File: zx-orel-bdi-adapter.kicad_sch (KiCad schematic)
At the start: 32 parts, among them J1 Barrel_Jack_Switch, J2 DB9_Male, SW1 SW_Push_Dual, SW2 SW_DPDT_x2, U1 74LS30, U2 74LS27, U3 74LS04, U4 74LS640, U5 28C256

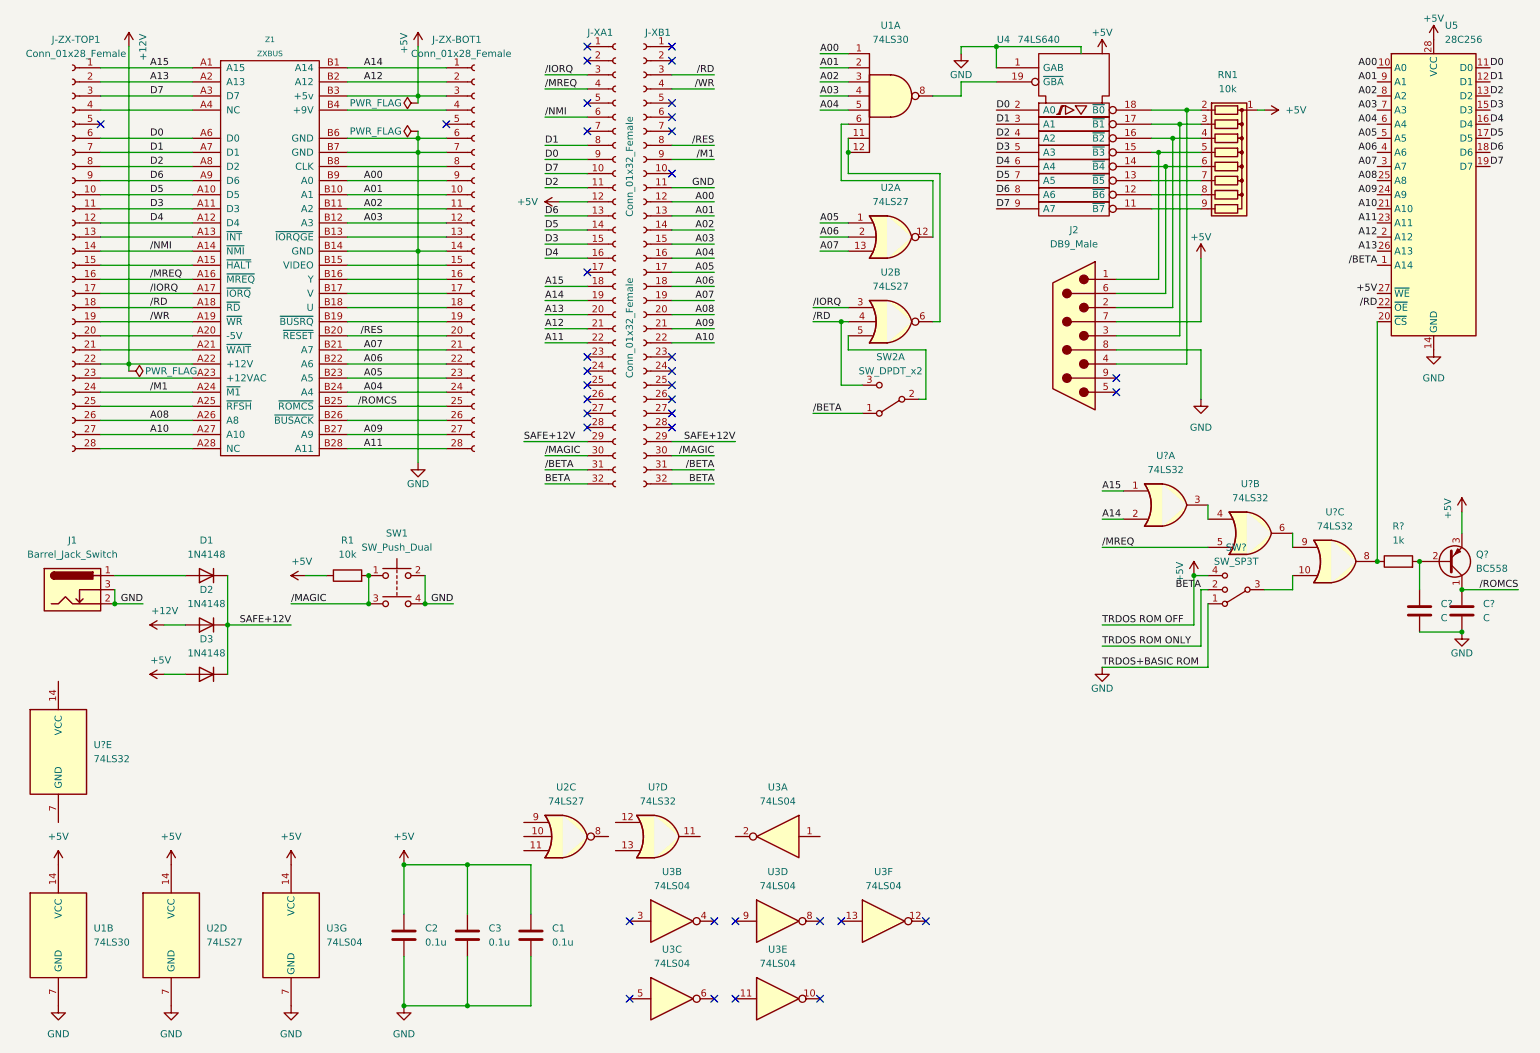
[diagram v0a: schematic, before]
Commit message: fixed romcs part
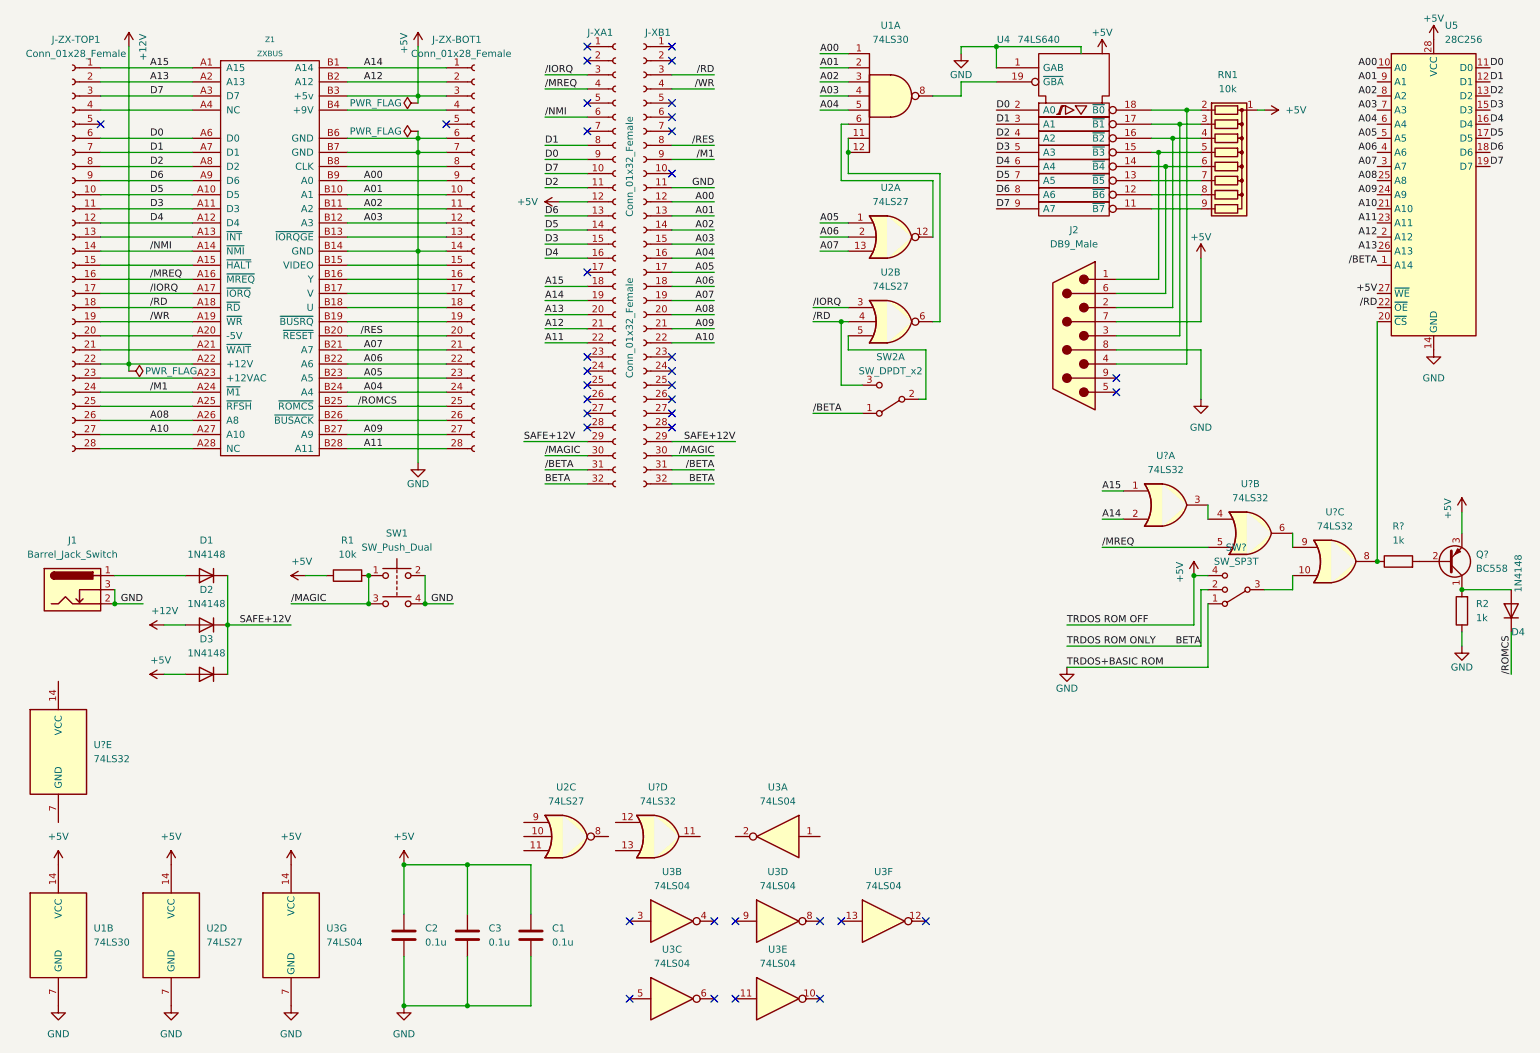
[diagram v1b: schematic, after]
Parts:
- removed C? (x2): C, symbol Device:C
- added D4: 1N4148, Diode_THT:D_DO-35_SOD27_P7.62mm_Horizontal, symbol Diode:1N4148
- added R2: 1k, symbol Device:R
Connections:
- net GND: now also R2.1
- net /ROMCS: now also D4.1 (K); no longer Q?.1 (C)
- new net: D4.2 (A), Q?.1 (C), R2.2

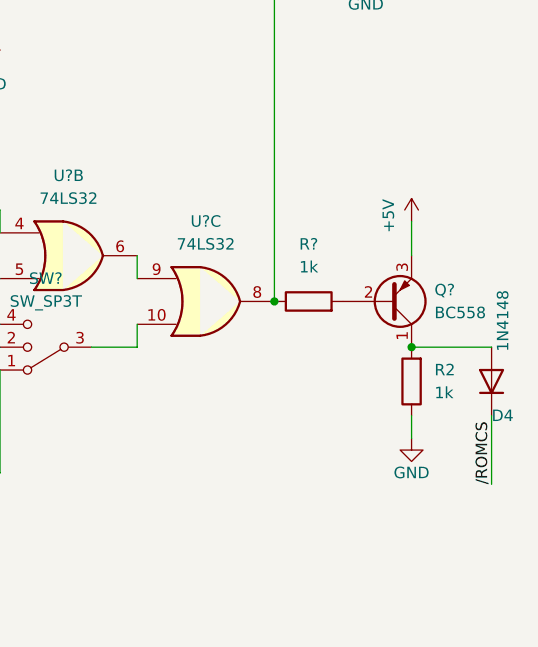
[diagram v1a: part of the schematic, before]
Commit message: changed bc558 schematic
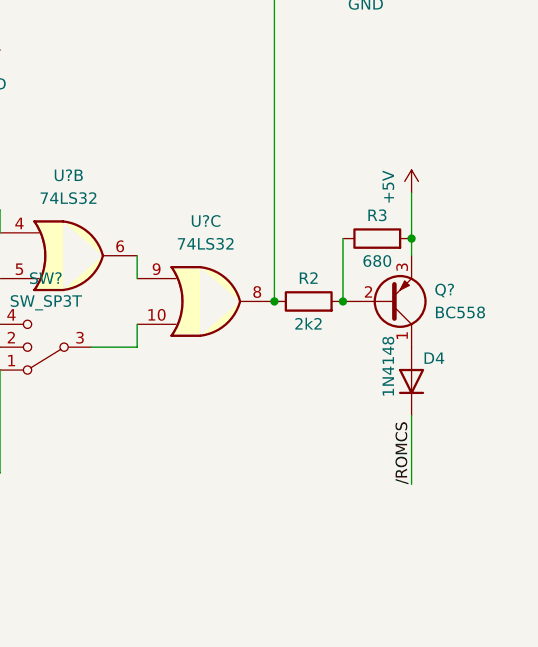
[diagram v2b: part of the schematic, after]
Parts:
- removed R?: 1k, symbol Device:R
- added R3: 680, symbol Device:R
- R2: value 1k -> 2k2
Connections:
- net +5V: now also R3.2
- net GND: no longer R2.1
- net at U5.20 (~{CS}), U?.8: now also R2.1
- net at Q?.2 (B): now also R2.2, R3.1
- net at D4.2 (A), Q?.1 (C): no longer R2.2
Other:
- moved on the sheet: D4
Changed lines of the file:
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@@
   (junction (at 85.09 38.1) (diameter 0) (color 0 0 0 0)
   )
+  (junction (at 265.43 111.76) (diameter 0) (color 0 0 0 0)
+  )
+  (junction (at 257.81 111.76) (diameter 0) (color 0 0 0 0)
+  )
   (junction (at 76.2 114.3) (diameter 0) (color 0 0 0 0)
   )
@@
   (junction (at 50.8 123.19) (diameter 0) (color 0 0 0 0)
   )
-  (junction (at 273.05 116.84) (diameter 0) (color 0 0 0 0)
+  (junction (at 273.05 104.775) (diameter 0) (color 0 0 0 0)
   )
   (junction (at 189.23 19.05) (diameter 0) (color 0 0 0 0)
@@
   )
   (junction (at 30.48 119.38) (diameter 0) (color 0 0 0 0)
-  )
-  (junction (at 257.81 111.76) (diameter 0) (color 0 0 0 0)
   )
   (junction (at 222.25 33.02) (diameter 0) (color 0 0 0 0)
@@
     (stroke (width 0) (type default))
   )
-  (wire (pts (xy 273.05 102.87) (xy 273.05 106.68))
-    (stroke (width 0) (type default))
-  )
   (wire (pts (xy 85.09 55.88) (xy 90.17 55.88))
     (stroke (width 0) (type default))
@@
     (stroke (width 0) (type default))
   )
+  (wire (pts (xy 273.05 99.695) (xy 273.05 104.775))
+    (stroke (width 0) (type default))
+  )
   (wire (pts (xy 27.94 78.74) (xy 44.45 78.74))
     (stroke (width 0) (type default))
   )
+  (wire (pts (xy 265.43 104.775) (xy 265.43 111.76))
+    (stroke (width 0) (type default))
+  )
   (wire (pts (xy 27.94 30.48) (xy 44.45 30.48))
     (stroke (width 0) (type default))
@@
     (stroke (width 0) (type default))
   )
-  (wire (pts (xy 281.94 132.08) (xy 281.94 124.46))
+  (wire (pts (xy 273.05 132.08) (xy 273.05 124.46))
     (stroke (width 0) (type default))
   )
@@
     (stroke (width 0) (type default))
   )
-  (wire (pts (xy 273.05 124.46) (xy 273.05 127))
-    (stroke (width 0) (type default))
-  )
   (wire (pts (xy 226.06 73.66) (xy 210.82 73.66))
     (stroke (width 0) (type default))
@@
     (stroke (width 0) (type default))
   )
-  (wire (pts (xy 281.94 116.84) (xy 273.05 116.84))
-    (stroke (width 0) (type default))
-  )
   (wire (pts (xy 107.95 44.45) (xy 115.57 44.45))
     (stroke (width 0) (type default))
@@
     (stroke (width 0) (type default))
   )
+  (wire (pts (xy 273.05 104.775) (xy 273.05 106.68))
+    (stroke (width 0) (type default))
+  )
   (wire (pts (xy 227.33 119.38) (xy 227.33 130.81))
     (stroke (width 0) (type default))
@@
     (effects (font (size 1.27 1.27)) (justify right bottom))
   )
-  (label "{slash}ROMCS" (at 281.94 132.08 90) (fields_autoplaced)
+  (label "{slash}ROMCS" (at 273.05 132.08 90) (fields_autoplaced)
     (effects (font (size 1.27 1.27)) (justify left bottom))
   )
@@
         (path "/02fab943-4e3a-413a-8dd4-a10cb6a6556c"
           (reference "#PWR0118") (unit 1)
-        )
-      )
-    )
-  )
-  (symbol (lib_id "power:GND") (at 273.05 127 0) (unit 1)
-    (in_bom yes) (on_board yes) (dnp no)
-    (property "Reference" "#PWR?" (at 273.05 133.35 0)
-      (effects (font (size 1.27 1.27)) hide)
-    )
-    (property "Value" "GND" (at 273.05 130.81 0)
-      (effects (font (size 1.27 1.27)))
-    )
-    (property "Footprint" "" (at 273.05 127 0)
-      (effects (font (size 1.27 1.27)) hide)
-    )
-    (property "Datasheet" "" (at 273.05 127 0)
-      (effects (font (size 1.27 1.27)) hide)
-    )
-    (pin "1")
-    (instances
-      (project "zx-orel-bdi-adapter"
-        (path "/02fab943-4e3a-413a-8dd4-a10cb6a6556c"
-          (reference "#PWR?") (unit 1)
         )
       )
@@
     )
   )
+  (symbol (lib_id "Device:R") (at 261.62 111.76 90) (unit 1)
+    (in_bom yes) (on_board yes) (dnp no)
+    (property "Reference" "R2" (at 261.62 109.22 90)
+      (effects (font (size 1.27 1.27)))
+    )
+    (property "Value" "2k2" (at 261.62 114.3 90)
+      (effects (font (size 1.27 1.27)))
+    )
+    (property "Footprint" "" (at 261.62 113.538 90)
+      (effects (font (size 1.27 1.27)) hide)
+    )
+    (property "Datasheet" "~" (at 261.62 111.76 0)
+      (effects (font (size 1.27 1.27)) hide)
+    )
+    (pin "1")
+    (pin "2")
+    (instances
+      (project "zx-orel-bdi-adapter"
+        (path "/02fab943-4e3a-413a-8dd4-a10cb6a6556c"
+          (reference "R2") (unit 1)
+        )
+      )
+    )
+  )
   (symbol (lib_id "Diode:1N4148") (at 46.99 114.3 180) (unit 1)
     (in_bom yes) (on_board yes) (dnp no) (fields_autoplaced)
@@
     )
   )
-  (symbol (lib_id "Device:R") (at 261.62 111.76 90) (unit 1)
-    (in_bom yes) (on_board yes) (dnp no) (fields_autoplaced)
-    (property "Reference" "R?" (at 261.62 105.41 90)
-      (effects (font (size 1.27 1.27)))
-    )
-    (property "Value" "1k" (at 261.62 107.95 90)
-      (effects (font (size 1.27 1.27)))
-    )
-    (property "Footprint" "" (at 261.62 113.538 90)
-      (effects (font (size 1.27 1.27)) hide)
-    )
-    (property "Datasheet" "~" (at 261.62 111.76 0)
+  (symbol (lib_id "Device:R") (at 269.24 104.775 90) (unit 1)
+    (in_bom yes) (on_board yes) (dnp no)
+    (property "Reference" "R3" (at 269.24 102.235 90)
+      (effects (font (size 1.27 1.27)))
+    )
+    (property "Value" "680" (at 269.24 107.315 90)
+      (effects (font (size 1.27 1.27)))
+    )
+    (property "Footprint" "" (at 269.24 106.553 90)
+      (effects (font (size 1.27 1.27)) hide)
+    )
+    (property "Datasheet" "~" (at 269.24 104.775 0)
       (effects (font (size 1.27 1.27)) hide)
     )
@@
       (project "zx-orel-bdi-adapter"
         (path "/02fab943-4e3a-413a-8dd4-a10cb6a6556c"
-          (reference "R?") (unit 1)
+          (reference "R3") (unit 1)
         )
       )
@@
     )
   )
-  (symbol (lib_id "power:+5V") (at 273.05 102.87 0) (unit 1)
+  (symbol (lib_id "power:+5V") (at 273.05 99.695 0) (unit 1)
     (in_bom yes) (on_board yes) (dnp no)
-    (property "Reference" "#PWR?" (at 273.05 106.68 0)
-      (effects (font (size 1.27 1.27)) hide)
-    )
-    (property "Value" "+5V" (at 270.51 104.14 90)
+    (property "Reference" "#PWR?" (at 273.05 103.505 0)
+      (effects (font (size 1.27 1.27)) hide)
+    )
+    (property "Value" "+5V" (at 270.51 100.965 90)
       (effects (font (size 1.27 1.27)) (justify left))
     )
-    (property "Footprint" "" (at 273.05 102.87 0)
-      (effects (font (size 1.27 1.27)) hide)
-    )
-    (property "Datasheet" "" (at 273.05 102.87 0)
+    (property "Footprint" "" (at 273.05 99.695 0)
+      (effects (font (size 1.27 1.27)) hide)
+    )
+    (property "Datasheet" "" (at 273.05 99.695 0)
       (effects (font (size 1.27 1.27)) hide)
     )
@@
     )
   )
-  (symbol (lib_id "Device:R") (at 273.05 120.65 180) (unit 1)
-    (in_bom yes) (on_board yes) (dnp no) (fields_autoplaced)
-    (property "Reference" "R2" (at 275.59 119.38 0)
-      (effects (font (size 1.27 1.27)) (justify right))
-    )
-    (property "Value" "1k" (at 275.59 121.92 0)
-      (effects (font (size 1.27 1.27)) (justify right))
-    )
-    (property "Footprint" "" (at 274.828 120.65 90)
-      (effects (font (size 1.27 1.27)) hide)
-    )
-    (property "Datasheet" "~" (at 273.05 120.65 0)
-      (effects (font (size 1.27 1.27)) hide)
-    )
-    (pin "1")
-    (pin "2")
-    (instances
-      (project "zx-orel-bdi-adapter"
-        (path "/02fab943-4e3a-413a-8dd4-a10cb6a6556c"
-          (reference "R2") (unit 1)
-        )
-      )
-    )
-  )
   (symbol (lib_id "74xx:74LS30") (at 170.18 27.94 0) (unit 1)
     (in_bom yes) (on_board yes) (dnp no) (fields_autoplaced)
@@
     )
   )
-  (symbol (lib_id "Diode:1N4148") (at 281.94 120.65 90) (unit 1)
+  (symbol (lib_id "Diode:1N4148") (at 273.05 120.65 90) (unit 1)
     (in_bom yes) (on_board yes) (dnp no)
-    (property "Reference" "D4" (at 281.94 124.46 90)
+    (property "Reference" "D4" (at 274.32 118.11 90)
       (effects (font (size 1.27 1.27)) (justify right))
     )
-    (property "Value" "1N4148" (at 283.21 110.49 0)
+    (property "Value" "1N4148" (at 270.51 115.57 0)
       (effects (font (size 1.27 1.27)) (justify right))
     )
-    (property "Footprint" "Diode_THT:D_DO-35_SOD27_P7.62mm_Horizontal" (at 281.94 120.65 0)
-      (effects (font (size 1.27 1.27)) hide)
-    )
-    (property "Datasheet" "https://assets.nexperia.com/documents/data-sheet/1N4148_1N4448.pdf" (at 281.94 120.65 0)
-      (effects (font (size 1.27 1.27)) hide)
-    )
+    (property "Footprint" "Diode_THT:D_DO-35_SOD27_P7.62mm_Horizontal" (at 273.05 120.65 0)
+      (effects (font (size 1.27 1.27)) hide)
+    )
+    (property "Datasheet" "https://assets.nexperia.com/documents/data-sheet/1N4148_1N4448.pdf" (at 273.05 120.65 0)
+      (effects (font (size 1.27 1.27)) hide)
+    )

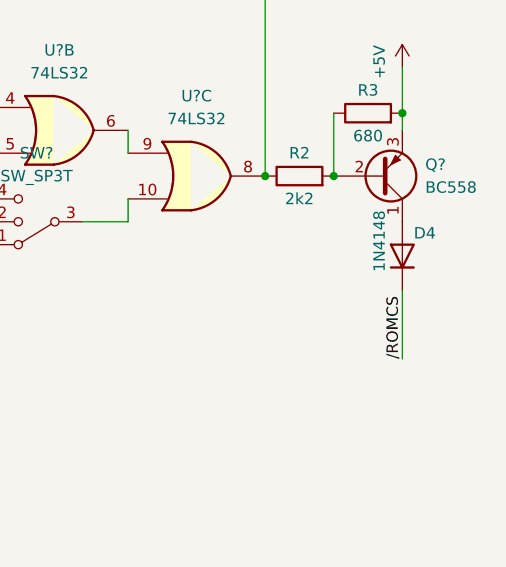
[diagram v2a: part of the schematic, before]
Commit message: fixed ROMCS activation schematic
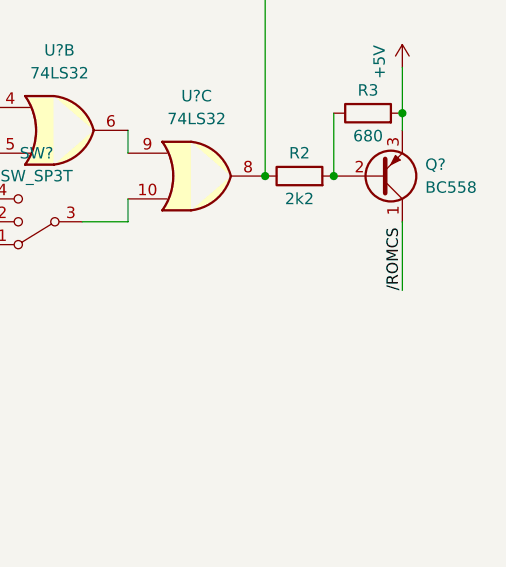
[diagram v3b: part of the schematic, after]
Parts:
- removed D4: 1N4148, Diode_THT:D_DO-35_SOD27_P7.62mm_Horizontal, symbol Diode:1N4148
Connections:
- net /ROMCS: now also Q?.1 (C)
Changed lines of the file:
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@@
     (stroke (width 0) (type default))
   )
-  (wire (pts (xy 273.05 132.08) (xy 273.05 124.46))
+  (wire (pts (xy 273.05 124.46) (xy 273.05 116.84))
     (stroke (width 0) (type default))
   )
@@
     (effects (font (size 1.27 1.27)) (justify right bottom))
   )
-  (label "{slash}ROMCS" (at 273.05 132.08 90) (fields_autoplaced)
+  (label "{slash}ROMCS" (at 273.05 124.46 90) (fields_autoplaced)
     (effects (font (size 1.27 1.27)) (justify left bottom))
   )
@@
         )
       )
-    )
-  )
-  (symbol (lib_id "Diode:1N4148") (at 273.05 120.65 90) (unit 1)
-    (in_bom yes) (on_board yes) (dnp no)
-    (property "Reference" "D4" (at 274.32 118.11 90)
-      (effects (font (size 1.27 1.27)) (justify right))
-    )
-    (property "Value" "1N4148" (at 270.51 115.57 0)
-      (effects (font (size 1.27 1.27)) (justify right))
-    )
-    (property "Footprint" "Diode_THT:D_DO-35_SOD27_P7.62mm_Horizontal" (at 273.05 120.65 0)
-      (effects (font (size 1.27 1.27)) hide)
-    )
-    (property "Datasheet" "https://assets.nexperia.com/documents/data-sheet/1N4148_1N4448.pdf" (at 273.05 120.65 0)
-      (effects (font (size 1.27 1.27)) hide)
-    )
-    (pin "1")
-    (pin "2")
-    (instances
-      (project "zx-orel-bdi-adapter"
-        (path "/02fab943-4e3a-413a-8dd4-a10cb6a6556c"
-          (reference "D4") (unit 1)
-        )
-      )
